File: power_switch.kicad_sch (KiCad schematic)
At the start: 35 parts, among them J1 XT90PW-M, J2 XT90PW-M, Q1 PSMN3R7-100BSEJ, Q2 PSMN3R7-100BSEJ, Q3 PSMN3R7-100BSEJ, Q4 PSMN3R7-100BSEJ, Q5 PSMN3R7-100BSEJ, Q6 PSMN3R7-100BSEJ, SW1 SW_SPST, U1 TPS2490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

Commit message: routing progress
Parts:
- R12: renamed from R14; footprint Resistor_SMD:R_1206_3216Metric_Pad1.30x1.75mm_HandSolder -> footprints:RES_PSR500_ROM
- R5: footprint Resistor_SMD:R_1206_3216Metric_Pad1.30x1.75mm_HandSolder -> footprints:RES_PSR500_ROM
- renumbered R12 to R10, R13 to R11, R15 to R13, R16 to R14, R17 to R15, R18 to R16
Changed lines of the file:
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@@
 		(dnp no)
 		(fields_autoplaced yes)
-		(property "Reference" "R18"
+		(property "Reference" "R16"
 			(at 275.59 52.0699 0)
 			(effects
@@
 			(project "doggie_board"
 				(path "/883cb7fa-3eb5-48d4-9cde-7c11307d94f0/7e8758ce-fdca-4bb6-a847-f546f03772b9"
-					(reference "R18")
+					(reference "R16")
 					(unit 1)
 				)
@@
 		(dnp no)
 		(fields_autoplaced yes)
-		(property "Reference" "#PWR018"
+		(property "Reference" "#PWR017"
 			(at 270.51 34.29 0)
 			(effects
@@
 			(project "doggie_board"
 				(path "/883cb7fa-3eb5-48d4-9cde-7c11307d94f0/7e8758ce-fdca-4bb6-a847-f546f03772b9"
-					(reference "#PWR018")
+					(reference "#PWR017")
 					(unit 1)
 				)
@@
 		(dnp no)
 		(fields_autoplaced yes)
-		(property "Reference" "R13"
+		(property "Reference" "R11"
 			(at 189.23 90.1699 0)
 			(effects
@@
 			(project "doggie_board"
 				(path "/883cb7fa-3eb5-48d4-9cde-7c11307d94f0/7e8758ce-fdca-4bb6-a847-f546f03772b9"
-					(reference "R13")
+					(reference "R11")
 					(unit 1)
 				)
@@
 		(dnp no)
 		(fields_autoplaced yes)
-		(property "Reference" "R16"
+		(property "Reference" "R14"
 			(at 246.38 45.7199 0)
 			(effects
@@
 			(project "doggie_board"
 				(path "/883cb7fa-3eb5-48d4-9cde-7c11307d94f0/7e8758ce-fdca-4bb6-a847-f546f03772b9"
-					(reference "R16")
+					(reference "R14")
 					(unit 1)
 				)
@@
 		(dnp no)
 		(fields_autoplaced yes)
-		(property "Reference" "R14"
+		(property "Reference" "R12"
 			(at 201.93 40.64 90)
 			(effects
@@
 			)
 		)
-		(property "Footprint" "Resistor_SMD:R_1206_3216Metric_Pad1.30x1.75mm_HandSolder"
+		(property "Footprint" "footprints:RES_PSR500_ROM"
 			(at 201.93 48.768 90)
 			(effects
@@
 			(project ""
 				(path "/883cb7fa-3eb5-48d4-9cde-7c11307d94f0/7e8758ce-fdca-4bb6-a847-f546f03772b9"
-					(reference "R14")
+					(reference "R12")
 					(unit 1)
 				)
@@
 		(dnp no)
 		(fields_autoplaced yes)
-		(property "Reference" "#PWR07"
+		(property "Reference" "#PWR04"
 			(at 67.31 67.31 0)
 			(effects
@@
 			(project "doggie_board"
 				(path "/883cb7fa-3eb5-48d4-9cde-7c11307d94f0/7e8758ce-fdca-4bb6-a847-f546f03772b9"
-					(reference "#PWR07")
+					(reference "#PWR04")
 					(unit 1)
 				)
@@
 		(dnp no)
 		(fields_autoplaced yes)
-		(property "Reference" "#FLG02"
+		(property "Reference" "#FLG01"
 			(at 57.15 50.165 0)
 			(effects
@@
 			(project "doggie_board"
 				(path "/883cb7fa-3eb5-48d4-9cde-7c11307d94f0/7e8758ce-fdca-4bb6-a847-f546f03772b9"
-					(reference "#FLG02")
+					(reference "#FLG01")
 					(unit 1)
 				)
@@
 		(dnp no)
 		(fields_autoplaced yes)
-		(property "Reference" "#PWR015"
+		(property "Reference" "#PWR014"
 			(at 193.04 67.31 0)
 			(effects
@@
 			(project "doggie_board"
 				(path "/883cb7fa-3eb5-48d4-9cde-7c11307d94f0/7e8758ce-fdca-4bb6-a847-f546f03772b9"
-					(reference "#PWR015")
+					(reference "#PWR014")
 					(unit 1)
 				)
@@
 		(dnp no)
 		(fields_autoplaced yes)
-		(property "Reference" "#PWR04"
+		(property "Reference" "#PWR010"
 			(at 162.56 129.54 0)
 			(effects
@@
 			(project "doggie_board"
 				(path "/883cb7fa-3eb5-48d4-9cde-7c11307d94f0/7e8758ce-fdca-4bb6-a847-f546f03772b9"
-					(reference "#PWR04")
+					(reference "#PWR010")
 					(unit 1)
 				)
@@
 		(dnp no)
 		(fields_autoplaced yes)
-		(property "Reference" "#PWR016"
+		(property "Reference" "#PWR015"
 			(at 209.55 102.87 0)
 			(effects
@@
 			(project "doggie_board"
 				(path "/883cb7fa-3eb5-48d4-9cde-7c11307d94f0/7e8758ce-fdca-4bb6-a847-f546f03772b9"
-					(reference "#PWR016")
+					(reference "#PWR015")
 					(unit 1)
 				)
@@
 		(dnp no)
 		(fields_autoplaced yes)
-		(property "Reference" "#PWR09"
+		(property "Reference" "#PWR06"
 			(at 87.63 97.79 0)
 			(effects
@@
 			(project "doggie_board"
 				(path "/883cb7fa-3eb5-48d4-9cde-7c11307d94f0/7e8758ce-fdca-4bb6-a847-f546f03772b9"
-					(reference "#PWR09")
+					(reference "#PWR06")
 					(unit 1)
 				)
@@
 		(dnp no)
 		(fields_autoplaced yes)
-		(property "Reference" "#PWR019"
+		(property "Reference" "#PWR018"
 			(at 273.05 68.58 0)
 			(effects
@@
 			(project "doggie_board"
 				(path "/883cb7fa-3eb5-48d4-9cde-7c11307d94f0/7e8758ce-fdca-4bb6-a847-f546f03772b9"
-					(reference "#PWR019")
+					(reference "#PWR018")
 					(unit 1)
 				)
@@
 		(dnp no)
 		(fields_autoplaced yes)
-		(property "Reference" "#PWR02"
+		(property "Reference" "#PWR01"
 			(at 39.37 88.9 0)
 			(effects
@@
 			(project "doggie_board"
 				(path "/883cb7fa-3eb5-48d4-9cde-7c11307d94f0/7e8758ce-fdca-4bb6-a847-f546f03772b9"
-					(reference "#PWR02")
+					(reference "#PWR01")
 					(unit 1)
 				)
@@
 		(dnp no)
 		(fields_autoplaced yes)
-		(property "Reference" "#PWR05"
+		(property "Reference" "#PWR02"
 			(at 49.53 63.5 0)
 			(effects
@@
 			(project "doggie_board"
 				(path "/883cb7fa-3eb5-48d4-9cde-7c11307d94f0/7e8758ce-fdca-4bb6-a847-f546f03772b9"
-					(reference "#PWR05")
+					(reference "#PWR02")
 					(unit 1)
 				)
@@
 		(dnp no)
 		(fields_autoplaced yes)
-		(property "Reference" "#PWR013"
+		(property "Reference" "#PWR011"
 			(at 175.26 63.5 0)
 			(effects
@@
 			(project "doggie_board"
 				(path "/883cb7fa-3eb5-48d4-9cde-7c11307d94f0/7e8758ce-fdca-4bb6-a847-f546f03772b9"
-					(reference "#PWR013")
+					(reference "#PWR011")
 					(unit 1)
 				)
@@
 		(dnp no)
 		(fields_autoplaced yes)
-		(property "Reference" "#PWR01"
+		(property "Reference" "#PWR012"
 			(at 177.8 127 0)
 			(effects
@@
 			(project "doggie_board"
 				(path "/883cb7fa-3eb5-48d4-9cde-7c11307d94f0/7e8758ce-fdca-4bb6-a847-f546f03772b9"
-					(reference "#PWR01")
+					(reference "#PWR012")
 					(unit 1)
 				)
@@
 		(dnp no)
 		(fields_autoplaced yes)
-		(property "Reference" "#PWR011"
+		(property "Reference" "#PWR08"
 			(at 147.32 68.58 0)
 			(effects
@@
 			(project "doggie_board"
 				(path "/883cb7fa-3eb5-48d4-9cde-7c11307d94f0/7e8758ce-fdca-4bb6-a847-f546f03772b9"
-					(reference "#PWR011")
+					(reference "#PWR08")
 					(unit 1)
 				)
@@
 		(dnp no)
 		(fields_autoplaced yes)
-		(property "Reference" "#PWR08"
+		(property "Reference" "#PWR05"
 			(at 83.82 102.87 0)
 			(effects
@@
 			(project "doggie_board"
 				(path "/883cb7fa-3eb5-48d4-9cde-7c11307d94f0/7e8758ce-fdca-4bb6-a847-f546f03772b9"
-					(reference "#PWR08")
+					(reference "#PWR05")
 					(unit 1)
 				)
@@
 		(dnp no)
 		(fields_autoplaced yes)
-		(property "Reference" "#PWR017"
+		(property "Reference" "#PWR016"
 			(at 213.36 97.79 0)
 			(effects
@@
 			(project "doggie_board"
 				(path "/883cb7fa-3eb5-48d4-9cde-7c11307d94f0/7e8758ce-fdca-4bb6-a847-f546f03772b9"
-					(reference "#PWR017")
+					(reference "#PWR016")
 					(unit 1)
 				)
@@
 		(dnp no)
 		(fields_autoplaced yes)
-		(property "Reference" "R12"
+		(property "Reference" "R10"
 			(at 189.23 81.2799 0)
 			(effects
@@
 			(project "doggie_board"
 				(path "/883cb7fa-3eb5-48d4-9cde-7c11307d94f0/7e8758ce-fdca-4bb6-a847-f546f03772b9"
-					(reference "R12")
+					(reference "R10")
 					(unit 1)
 				)
@@
 		(dnp no)
 		(fields_autoplaced yes)
-		(property "Reference" "R17"
+		(property "Reference" "R15"
 			(at 266.7 45.7199 0)
 			(effects
@@
 			(project "doggie_board"
 				(path "/883cb7fa-3eb5-48d4-9cde-7c11307d94f0/7e8758ce-fdca-4bb6-a847-f546f03772b9"
-					(reference "R17")
+					(reference "R15")
 					(unit 1)
 				)
@@
 		(dnp no)
 		(fields_autoplaced yes)
-		(property "Reference" "#PWR03"
+		(property "Reference" "#PWR09"
 			(at 162.56 113.03 0)
 			(effects
@@
 			(project "doggie_board"
 				(path "/883cb7fa-3eb5-48d4-9cde-7c11307d94f0/7e8758ce-fdca-4bb6-a847-f546f03772b9"
-					(reference "#PWR03")
+					(reference "#PWR09")
 					(unit 1)
 				)
@@
 		(dnp no)
 		(fields_autoplaced yes)
-		(property "Reference" "#PWR06"
+		(property "Reference" "#PWR03"
 			(at 60.96 102.87 0)
 			(effects
@@
 			(project "doggie_board"
 				(path "/883cb7fa-3eb5-48d4-9cde-7c11307d94f0/7e8758ce-fdca-4bb6-a847-f546f03772b9"
-					(reference "#PWR06")
+					(reference "#PWR03")
 					(unit 1)
 				)
@@
 		(dnp no)
 		(fields_autoplaced yes)
-		(property "Reference" "#FLG01"
+		(property "Reference" "#FLG02"
 			(at 177.8 118.745 0)
 			(effects
@@
 			(project "doggie_board"
 				(path "/883cb7fa-3eb5-48d4-9cde-7c11307d94f0/7e8758ce-fdca-4bb6-a847-f546f03772b9"
-					(reference "#FLG01")
+					(reference "#FLG02")
 					(unit 1)
 				)
@@
 		(dnp no)
 		(fields_autoplaced yes)
-		(property "Reference" "R15"
+		(property "Reference" "R13"
 			(at 226.06 45.7199 0)
 			(effects
@@
 			(project "doggie_board"
 				(path "/883cb7fa-3eb5-48d4-9cde-7c11307d94f0/7e8758ce-fdca-4bb6-a847-f546f03772b9"
-					(reference "R15")
+					(reference "R13")
 					(unit 1)
 				)
@@
 		(dnp no)
 		(fields_autoplaced yes)
-		(property "Reference" "#PWR010"
+		(property "Reference" "#PWR07"
 			(at 144.78 34.29 0)
 			(effects
@@
 			(project "doggie_board"
 				(path "/883cb7fa-3eb5-48d4-9cde-7c11307d94f0/7e8758ce-fdca-4bb6-a847-f546f03772b9"
-					(reference "#PWR010")
+					(reference "#PWR07")
 					(unit 1)
 				)
@@
 		(dnp no)
 		(fields_autoplaced yes)
-		(property "Reference" "#PWR014"
+		(property "Reference" "#PWR013"
 			(at 186.69 102.87 0)
 			(effects
@@
 			(project "doggie_board"
 				(path "/883cb7fa-3eb5-48d4-9cde-7c11307d94f0/7e8758ce-fdca-4bb6-a847-f546f03772b9"
-					(reference "#PWR014")
+					(reference "#PWR013")
 					(unit 1)
 				)
@@
 			)
 		)
-		(property "Footprint" "Resistor_SMD:R_1206_3216Metric_Pad1.30x1.75mm_HandSolder"
+		(property "Footprint" "footprints:RES_PSR500_ROM"
 			(at 76.2 48.768 90)
 			(effects

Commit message: transistor pins
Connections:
- net drain_left: now also Q1.2, Q2.2, Q3.2; no longer Q1.MB, Q2.MB, Q3.MB
- net drain_r: now also Q4.2, Q5.2, Q6.2; no longer Q4.MB, Q5.MB, Q6.MB

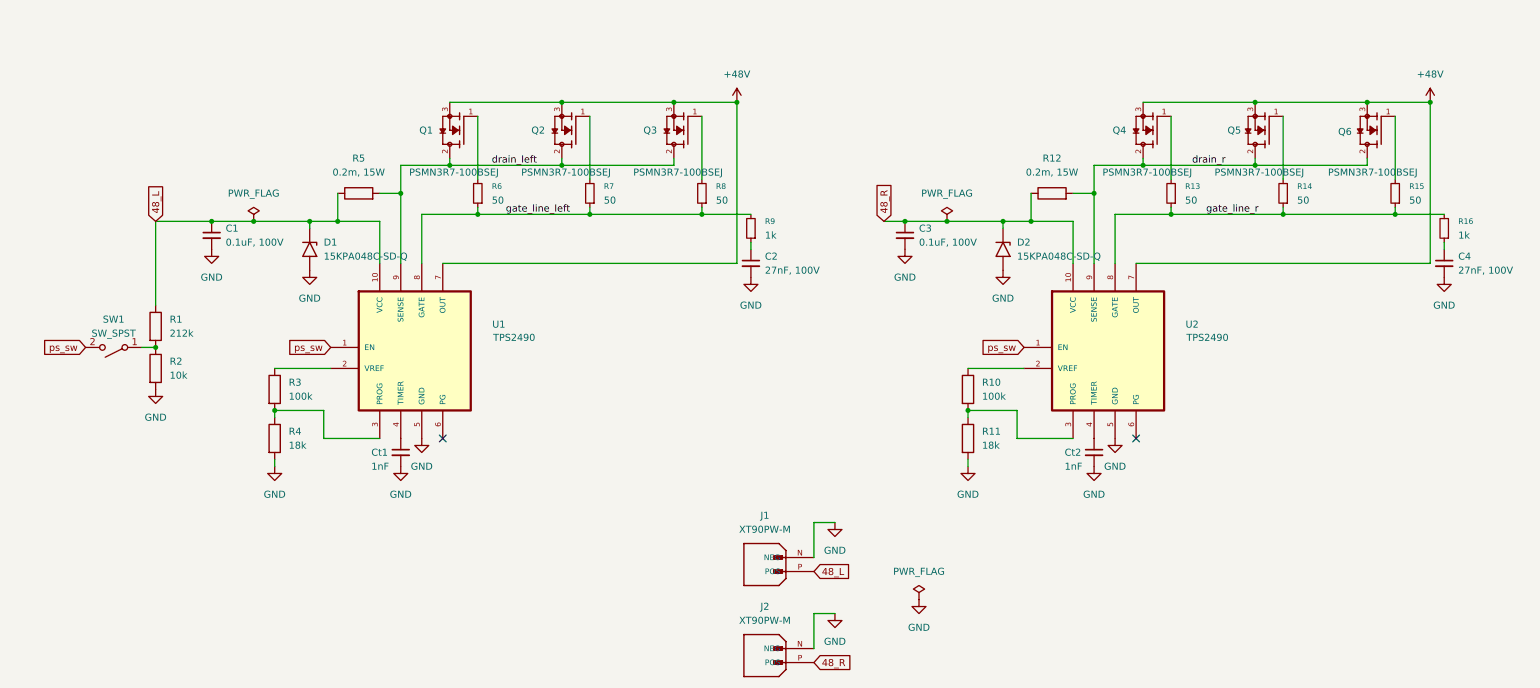
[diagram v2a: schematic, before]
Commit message: swapped left and right
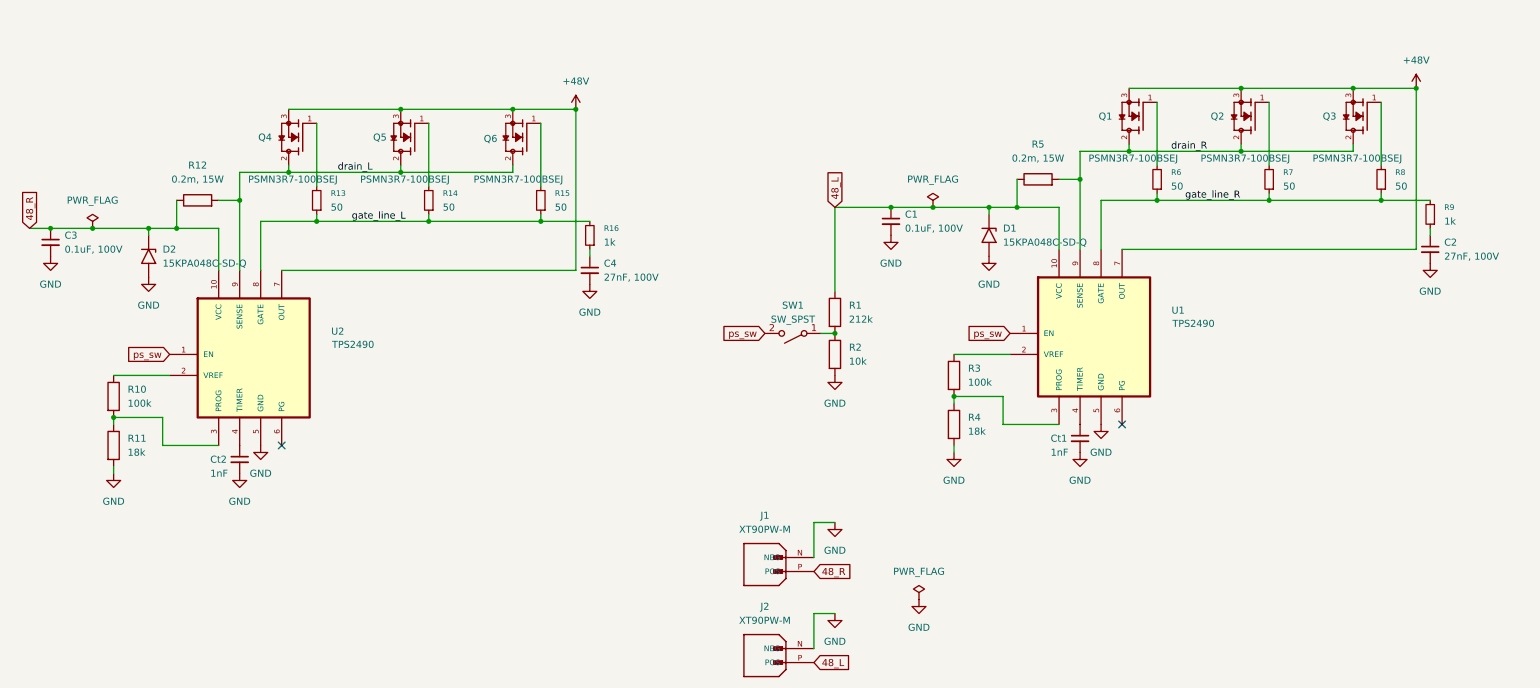
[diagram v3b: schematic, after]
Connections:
- net 48_L: now also J2.P (POS); no longer J1.P (POS)
- net 48_R: now also J1.P (POS); no longer J2.P (POS)
- net drain_left renamed drain_R
- net drain_r renamed drain_L
- net gate_line_left renamed gate_line_R
- net gate_line_r renamed gate_line_L
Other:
- moved on the sheet: C1, C2, C3, C4, Ct1, Ct2, D1, D2, Q1, Q2, Q3, Q4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

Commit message: Fixed Schematics with more cost effective IC's
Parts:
- removed C3: 0.1uF, 100V, Capacitor_SMD:C_1206_3216Metric_Pad1.33x1.80mm_HandSolder, symbol Device:C_Small
- removed C4: 27nF, 100V, Capacitor_SMD:C_1206_3216Metric_Pad1.33x1.80mm_HandSolder, symbol Device:C_Small
- removed Ct2: 1nF, Capacitor_SMD:C_0805_2012Metric_Pad1.18x1.45mm_HandSolder, symbol Device:C_Small
- removed D2: 15KPA048C-SD-Q, footprints:DIODE_15KPA048C-SD-Q_BRN, symbol Diode:SMF48A
- removed R10: 100k, Resistor_SMD:R_0201_0603Metric_Pad0.64x0.40mm_HandSolder, symbol Device:R
- removed R11: 18k, Resistor_SMD:R_0201_0603Metric_Pad0.64x0.40mm_HandSolder, symbol Device:R
- removed R12: 0.2m, 15W, footprints:RES_PSR500_ROM, symbol Device:R
- removed R13, R14, R15: 50, Resistor_SMD:R_1206_3216Metric_Pad1.30x1.75mm_HandSolder, symbol Device:R_Small
- removed R16: 1k, Resistor_SMD:R_1206_3216Metric_Pad1.30x1.75mm_HandSolder, symbol Device:R_Small
- removed U2: TPS2490, Package_SO:VSSOP-10_3x3mm_P0.5mm, symbol tps2490g:TPS2490DGSR
- added J1: Conn_01x02, Connector_PinHeader_2.54mm:PinHeader_1x02_P2.54mm_Vertical, symbol Connector_Generic:Conn_01x02
- added R10, R11, R9: 50, Resistor_SMD:R_1206_3216Metric_Pad1.30x1.75mm_HandSolder, symbol Device:R_Small
- C1: value 0.1uF, 100V -> 0.1u, 100V
- C2: value 27nF, 100V -> 27n, 100V
- Ct1: value 1nF -> 1n
- Q1, Q2, Q3, Q4, Q5, Q6: footprint Package_TO_SOT_SMD:TO-263-2 -> footprints:D2PAK_NEX
- renumbered J1 to J2, J2 to J3, R9 to R12
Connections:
- net 48_R is gone; now on net 48_RAW: J2.P (POS)
- net drain_R is gone; now on net drain_line: Q1.2, Q2.2, Q3.2, R5.2, U1.9 (SENSE)
- net GND: now also J1.2 (Pin_2)
- net at Q5.1: now also R10.2
- net 48V_PG: now reaches U1.6 (PG)
- net at Q6.1: now also R11.2
- net sw_low: now reaches R1.2, R2.1, SW1.1 (A)
- net sw_low: now also J1.1 (Pin_1)
- net at Q4.1: now also R9.2
- net 48_L renamed 48_RAW
- net drain_L renamed drain_line
- net gate_line_R renamed gate_line
- net gate_line: now also R10.1, R11.1, R9.1
- no-connect marks 2 -> 0
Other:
- moved on the sheet: C1, C2, Ct1, D1, J2, J3, Q1, Q2, Q3, R1, R12, R2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

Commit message: feat: added footprints
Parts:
- C1, C2: footprint Capacitor_SMD:C_1206_3216Metric_Pad1.33x1.80mm_HandSolder -> Capacitor_SMD:C_0201_0603Metric_Pad0.64x0.40mm_HandSolder
- Ct1: footprint Capacitor_SMD:C_0805_2012Metric_Pad1.18x1.45mm_HandSolder -> Capacitor_SMD:C_0201_0603Metric_Pad0.64x0.40mm_HandSolder
- R10, R11, R6, R7, R8, R9: value 50 -> 60; footprint Resistor_SMD:R_1206_3216Metric_Pad1.30x1.75mm_HandSolder -> Resistor_SMD:R_0201_0603Metric_Pad0.64x0.40mm_HandSolder
- R12: footprint Resistor_SMD:R_1206_3216Metric_Pad1.30x1.75mm_HandSolder -> Resistor_SMD:R_0201_0603Metric_Pad0.64x0.40mm_HandSolder
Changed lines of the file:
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@@
 			)
 		)
-		(property "Value" "50"
+		(property "Value" "60"
 			(at 130.81 50.7999 0)
 			(effects
@@
 			)
 		)
-		(property "Footprint" "Resistor_SMD:R_1206_3216Metric_Pad1.30x1.75mm_HandSolder"
+		(property "Footprint" "Resistor_SMD:R_0201_0603Metric_Pad0.64x0.40mm_HandSolder"
 			(at 128.27 49.53 0)
 			(effects
@@
 			)
 		)
-		(property "Value" "50"
+		(property "Value" "60"
 			(at 184.15 49.5299 0)
 			(effects
@@
 			)
 		)
-		(property "Footprint" "Resistor_SMD:R_1206_3216Metric_Pad1.30x1.75mm_HandSolder"
+		(property "Footprint" "Resistor_SMD:R_0201_0603Metric_Pad0.64x0.40mm_HandSolder"
 			(at 181.61 48.26 0)
 			(effects
@@
 			)
 		)
-		(property "Footprint" "Capacitor_SMD:C_0805_2012Metric_Pad1.18x1.45mm_HandSolder"
+		(property "Footprint" "Capacitor_SMD:C_0201_0603Metric_Pad0.64x0.40mm_HandSolder"
 			(at 101.6 96.52 0)
 			(effects
@@
 			)
 		)
-		(property "Footprint" "Resistor_SMD:R_1206_3216Metric_Pad1.30x1.75mm_HandSolder"
+		(property "Footprint" "Resistor_SMD:R_0201_0603Metric_Pad0.64x0.40mm_HandSolder"
 			(at 193.04 55.88 0)
 			(effects
@@
 			)
 		)
-		(property "Footprint" "Capacitor_SMD:C_1206_3216Metric_Pad1.33x1.80mm_HandSolder"
+		(property "Footprint" "Capacitor_SMD:C_0201_0603Metric_Pad0.64x0.40mm_HandSolder"
 			(at 67.31 57.15 0)
 			(effects
@@
 			)
 		)
-		(property "Footprint" "Capacitor_SMD:C_1206_3216Metric_Pad1.33x1.80mm_HandSolder"
+		(property "Footprint" "Capacitor_SMD:C_0201_0603Metric_Pad0.64x0.40mm_HandSolder"
 			(at 193.04 62.23 0)
 			(effects
@@
 			)
 		)
-		(property "Value" "50"
+		(property "Value" "60"
 			(at 146.05 50.7999 0)
 			(effects
@@
 			)
 		)
-		(property "Footprint" "Resistor_SMD:R_1206_3216Metric_Pad1.30x1.75mm_HandSolder"
+		(property "Footprint" "Resistor_SMD:R_0201_0603Metric_Pad0.64x0.40mm_HandSolder"
 			(at 143.51 49.53 0)
 			(effects
@@
 			)
 		)
-		(property "Value" "50"
+		(property "Value" "60"
 			(at 172.72 49.5299 0)
 			(effects
@@
 			)
 		)
-		(property "Footprint" "Resistor_SMD:R_1206_3216Metric_Pad1.30x1.75mm_HandSolder"
+		(property "Footprint" "Resistor_SMD:R_0201_0603Metric_Pad0.64x0.40mm_HandSolder"
 			(at 170.18 48.26 0)
 			(effects
@@
 			)
 		)
-		(property "Value" "50"
+		(property "Value" "60"
 			(at 119.38 50.7999 0)
 			(effects
@@
 			)
 		)
-		(property "Footprint" "Resistor_SMD:R_1206_3216Metric_Pad1.30x1.75mm_HandSolder"
+		(property "Footprint" "Resistor_SMD:R_0201_0603Metric_Pad0.64x0.40mm_HandSolder"
 			(at 116.84 49.53 0)
 			(effects
@@
 			)
 		)
-		(property "Value" "50"
+		(property "Value" "60"
 			(at 157.48 50.7999 0)
 			(effects
@@
 			)
 		)
-		(property "Footprint" "Resistor_SMD:R_1206_3216Metric_Pad1.30x1.75mm_HandSolder"
+		(property "Footprint" "Resistor_SMD:R_0201_0603Metric_Pad0.64x0.40mm_HandSolder"
 			(at 154.94 49.53 0)
 			(effects

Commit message: added headers and modified some stuff
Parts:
- removed J1: Conn_01x02, Connector_PinHeader_2.54mm:PinHeader_1x02_P2.54mm_Vertical, symbol Connector_Generic:Conn_01x02
- added J1: Conn_01x03, symbol Connector_Generic:Conn_01x03
- added J4: Conn_01x02, symbol Connector_Generic:Conn_01x02
- added Q9: 2N7002, Package_TO_SOT_SMD:SOT-23, symbol Transistor_FET:2N7002
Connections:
- net 48V_PG: now also J4.1 (Pin_1)
- net GND: now also J1.3 (Pin_3), J4.2 (Pin_2)
- net sw_low: now also J1.1 (Pin_1), Q9.3 (D); no longer SW1.1 (A)
- new net: J1.2 (Pin_2), Q9.1 (G)
- new net: Q9.2 (S), SW1.1 (A)
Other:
- note added: "R1 and R2 set undervoltage so we should keep that feedback so I added a NMOS to switch EN optionally 1 and 2 can be bridged if external enable is not used"
- note added: "Simple power good connector that can be used with external pullup"
- moved on the sheet: SW1

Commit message: added footprints and standardized EN headers
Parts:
- J1: footprint (none) -> Connector_PinHeader_2.54mm:PinHeader_1x03_P2.54mm_Vertical
- J4: footprint (none) -> Connector_PinHeader_2.54mm:PinHeader_1x02_P2.54mm_Vertical
- SW1: footprint (none) -> Button_Switch_THT:SW_PUSH_6mm
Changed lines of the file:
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@@
 			)
 		)
-		(property "Footprint" ""
+		(property "Footprint" "Connector_PinHeader_2.54mm:PinHeader_1x03_P2.54mm_Vertical"
 			(at 43.18 96.52 0)
 			(effects
@@
 			)
 		)
-		(property "Footprint" ""
+		(property "Footprint" "Connector_PinHeader_2.54mm:PinHeader_1x02_P2.54mm_Vertical"
 			(at 132.08 68.58 0)
 			(effects
@@
 			)
 		)
-		(property "Footprint" ""
+		(property "Footprint" "Button_Switch_THT:SW_PUSH_6mm"
 			(at 33.02 77.47 0)
 			(effects

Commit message: pcb routing
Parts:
- added D2: 5.0SMDJ58A, Diode_SMD:D_SMB-SMC_Universal_Handsoldering, symbol Diode:SMF48A
- D1: value 15KPA048C-SD-Q -> 5.0SMDJ58A; footprint footprints:DIODE_15KPA048C-SD-Q_BRN -> Diode_SMD:D_SMB-SMC_Universal_Handsoldering
- R1: value 212k -> 300k
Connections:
- net 48_RAW: now also D2.1 (A1)
- net GND: now also D2.2 (A2)
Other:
- moved on the sheet: D1, J2, J3
